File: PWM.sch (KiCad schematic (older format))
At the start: 11 parts, among them U2 MCP6004

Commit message: Rev A
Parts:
- R10: value 43k -> 30k
- R11: value 24k -> 15k
- R8: value 24k -> 30k
- RV1: value 10k -> 100
- RV2: value 10k -> 1k
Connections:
- net VCC: now also R10.1; no longer RV2.1, RV2.2
- net VIN: now also R8.1; no longer RV1.1, RV1.2
- net VIN_DIV: now also RV1.2; no longer R8.2, R9.1
- net VREF: now also RV2.2; no longer R10.2, R11.1
- net BUF_OUT renamed BUF
- net VIN_ADJ renamed VIN_ADJ_M
- net VIN_ADJ_M: now also R9.1; no longer R8.1
- net VREF_ADJ renamed VREF_ADJ_M
- net VREF_ADJ_M: now also R11.1; no longer R10.1
- new net VIN_ADJ_P: R8.2, RV1.1
- new net VREF_ADJ_P: R10.2, RV2.1
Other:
- moved on the sheet: R10, R8, R9, RV1, RV2
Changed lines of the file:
@@
 Text HLabel 5150 1400 0    60   Input ~ 0
 SAWTOOTH
-Text HLabel 2300 1750 0    60   Input ~ 0
+Text HLabel 2300 1800 0    60   Input ~ 0
 VIN
 $Comp
@@
 AR Path="/59C03855/59C00B33" Ref="R35"  Part="1"
 F 0 "R11" V 3230 2400 50  0000 C CNN
-F 1 "24k" V 3150 2400 50  0000 C CNN
+F 1 "15k" V 3150 2400 50  0000 C CNN
 F 2 "olof:R_0805_HandSoldering" V 3080 2400 50  0001 C CNN
 F 3 "" H 3150 2400 50  0000 C CNN
@@
 L R R10
 U 1 1 59C00B88
-P 3150 2000
+P 3150 950
 AR Path="/59C00A8D/59C00B88" Ref="R10"  Part="1"
 AR Path="/59C037F5/59C00B88" Ref="R18"  Part="1"
 AR Path="/59C0381C/59C00B88" Ref="R26"  Part="1"
 AR Path="/59C03855/59C00B88" Ref="R34"  Part="1"
-F 0 "R10" V 3230 2000 50  0000 C CNN
-F 1 "43k" V 3150 2000 50  0000 C CNN
-F 2 "olof:R_0805_HandSoldering" V 3080 2000 50  0001 C CNN
-F 3 "" H 3150 2000 50  0000 C CNN
-F 4 "1208710" V 3150 2000 60  0001 C CNN "Part"
-	1    3150 2000
-	1    0    0    -1
-$EndComp
-Wire Wire Line
-	3150 2150 3150 2250
+F 0 "R10" V 3230 950 50  0000 C CNN
+F 1 "30k" V 3150 950 50  0000 C CNN
+F 2 "olof:R_0805_HandSoldering" V 3080 950 50  0001 C CNN
+F 3 "" H 3150 950 50  0000 C CNN
+F 4 "1208710" V 3150 950 60  0001 C CNN "Part"
+	1    3150 950
+	1    0    0    -1
+$EndComp
+Wire Wire Line
+	3150 1750 3150 2250
 $Comp
 L GND #PWR040
 U 1 1 59C00BB9
-P 3150 2600
+P 3150 2650
 AR Path="/59C00A8D/59C00BB9" Ref="#PWR040"  Part="1"
 AR Path="/59C037F5/59C00BB9" Ref="#PWR047"  Part="1"
 AR Path="/59C0381C/59C00BB9" Ref="#PWR054"  Part="1"
 AR Path="/59C03855/59C00BB9" Ref="#PWR061"  Part="1"
-F 0 "#PWR061" H 3150 2350 50  0001 C CNN
-F 1 "GND" H 3150 2450 50  0000 C CNN
-F 2 "" H 3150 2600 50  0000 C CNN
-F 3 "" H 3150 2600 50  0000 C CNN
-	1    3150 2600
+F 0 "#PWR040" H 3150 2400 50  0001 C CNN
+F 1 "GND" H 3150 2500 50  0000 C CNN
+F 2 "" H 3150 2650 50  0000 C CNN
+F 3 "" H 3150 2650 50  0000 C CNN
+	1    3150 2650
 	1    0    0    -1
 $EndComp
@@
 L VCC #PWR041
 U 1 1 59C00BD3
-P 3150 1100
+P 3150 750
 AR Path="/59C00A8D/59C00BD3" Ref="#PWR041"  Part="1"
 AR Path="/59C037F5/59C00BD3" Ref="#PWR048"  Part="1"
 AR Path="/59C0381C/59C00BD3" Ref="#PWR055"  Part="1"
 AR Path="/59C03855/59C00BD3" Ref="#PWR062"  Part="1"
-F 0 "#PWR062" H 3150 950 50  0001 C CNN
-F 1 "VCC" H 3150 1250 50  0000 C CNN
-F 2 "" H 3150 1100 50  0000 C CNN
-F 3 "" H 3150 1100 50  0000 C CNN
-	1    3150 1100
-	1    0    0    -1
-$EndComp
-Wire Wire Line
-	3150 1500 3150 1850
-Wire Wire Line
-	3150 2550 3150 2600
-Wire Wire Line
-	3150 2200 3750 2200
-Wire Wire Line
-	3750 2200 3750 2750
+F 0 "#PWR041" H 3150 600 50  0001 C CNN
+F 1 "VCC" H 3150 900 50  0000 C CNN
+F 2 "" H 3150 750 50  0000 C CNN
+F 3 "" H 3150 750 50  0000 C CNN
+	1    3150 750
+	1    0    0    -1
+$EndComp
+Wire Wire Line
+	3150 2550 3150 2650
+Wire Wire Line
+	3750 1600 3750 2750
 Wire Wire Line
 	3750 2750 4050 2750
-Connection ~ 3150 2200
 $Comp
 L R R8
 U 1 1 59C00D17
-P 2500 2750
+P 2500 2100
 AR Path="/59C00A8D/59C00D17" Ref="R8"  Part="1"
 AR Path="/59C037F5/59C00D17" Ref="R16"  Part="1"
 AR Path="/59C0381C/59C00D17" Ref="R24"  Part="1"
 AR Path="/59C03855/59C00D17" Ref="R32"  Part="1"
-F 0 "R8" V 2580 2750 50  0000 C CNN
-F 1 "24k" V 2500 2750 50  0000 C CNN
-F 2 "olof:R_0805_HandSoldering" V 2430 2750 50  0001 C CNN
-F 3 "" H 2500 2750 50  0000 C CNN
-	1    2500 2750
+F 0 "R8" V 2580 2100 50  0000 C CNN
+F 1 "30k" V 2500 2100 50  0000 C CNN
+F 2 "olof:R_0805_HandSoldering" V 2430 2100 50  0001 C CNN
+F 3 "" H 2500 2100 50  0000 C CNN
+	1    2500 2100
 	1    0    0    -1
 $EndComp
@@
 L R R9
 U 1 1 59C00DEF
-P 2500 3150
+P 2500 3700
 AR Path="/59C00A8D/59C00DEF" Ref="R9"  Part="1"
 AR Path="/59C037F5/59C00DEF" Ref="R17"  Part="1"
 AR Path="/59C0381C/59C00DEF" Ref="R25"  Part="1"
 AR Path="/59C03855/59C00DEF" Ref="R33"  Part="1"
-F 0 "R9" V 2580 3150 50  0000 C CNN
-F 1 "470" V 2500 3150 50  0000 C CNN
-F 2 "olof:R_0805_HandSoldering" V 2430 3150 50  0001 C CNN
-F 3 "" H 2500 3150 50  0000 C CNN
-F 4 "1208662" V 2500 3150 60  0001 C CNN "Part"
-	1    2500 3150
-	1    0    0    -1
-$EndComp
-Wire Wire Line
-	2500 2900 2500 3000
-Connection ~ 2500 2950
+F 0 "R9" V 2580 3700 50  0000 C CNN
+F 1 "470" V 2500 3700 50  0000 C CNN
+F 2 "olof:R_0805_HandSoldering" V 2430 3700 50  0001 C CNN
+F 3 "" H 2500 3700 50  0000 C CNN
+F 4 "1208662" V 2500 3700 60  0001 C CNN "Part"
+	1    2500 3700
+	1    0    0    -1
+$EndComp
 $Comp
 L GND #PWR042
 U 1 1 59C00E40
-P 2500 3350
+P 2500 3900
 AR Path="/59C00A8D/59C00E40" Ref="#PWR042"  Part="1"
 AR Path="/59C037F5/59C00E40" Ref="#PWR049"  Part="1"
 AR Path="/59C0381C/59C00E40" Ref="#PWR056"  Part="1"
 AR Path="/59C03855/59C00E40" Ref="#PWR063"  Part="1"
-F 0 "#PWR063" H 2500 3100 50  0001 C CNN
-F 1 "GND" H 2500 3200 50  0000 C CNN
-F 2 "" H 2500 3350 50  0000 C CNN
-F 3 "" H 2500 3350 50  0000 C CNN
-	1    2500 3350
-	1    0    0    -1
-$EndComp
-Wire Wire Line
-	2500 3300 2500 3350
-Wire Wire Line
-	2500 2300 2500 2600
+F 0 "#PWR042" H 2500 3650 50  0001 C CNN
+F 1 "GND" H 2500 3750 50  0000 C CNN
+F 2 "" H 2500 3900 50  0000 C CNN
+F 3 "" H 2500 3900 50  0000 C CNN
+	1    2500 3900
+	1    0    0    -1
+$EndComp
+Wire Wire Line
+	2500 3850 2500 3900
 $Comp
 L VCC #PWR043
@@
 AR Path="/59C0381C/59C00F65" Ref="#PWR057"  Part="1"
 AR Path="/59C03855/59C00F65" Ref="#PWR064"  Part="1"
-F 0 "#PWR064" H 4250 2350 50  0001 C CNN
+F 0 "#PWR043" H 4250 2350 50  0001 C CNN
 F 1 "VCC" H 4250 2650 50  0000 C CNN
 F 2 "" H 4250 2500 50  0000 C CNN
@@
 AR Path="/59C0381C/59C00F93" Ref="#PWR058"  Part="1"
 AR Path="/59C03855/59C00F93" Ref="#PWR065"  Part="1"
-F 0 "#PWR065" H 4250 2950 50  0001 C CNN
+F 0 "#PWR044" H 4250 2950 50  0001 C CNN
 F 1 "GND" H 4250 3050 50  0000 C CNN
 F 2 "" H 4250 3200 50  0000 C CNN
@@
 $EndComp
 Wire Wire Line
-	3000 2950 2500 2950
-Wire Wire Line
 	3300 2950 4050 2950
 $Comp
@@
 	5000 2850 5000 3550
 Wire Wire Line
-	5000 3550 4400 3550
+	4400 3550 7100 3550
 $Comp
 L MCP6004 U2
@@
 AR Path="/59C0381C/59C015C7" Ref="#PWR059"  Part="1"
 AR Path="/59C03855/59C015C7" Ref="#PWR066"  Part="1"
-F 0 "#PWR066" H 5850 2250 50  0001 C CNN
+F 0 "#PWR045" H 5850 2250 50  0001 C CNN
 F 1 "VCC" H 5850 2550 50  0000 C CNN
 F 2 "" H 5850 2400 50  0000 C CNN
@@
 AR Path="/59C0381C/59C0160F" Ref="#PWR060"  Part="1"
 AR Path="/59C03855/59C0160F" Ref="#PWR067"  Part="1"
-F 0 "#PWR067" H 5850 2850 50  0001 C CNN
+F 0 "#PWR046" H 5850 2850 50  0001 C CNN
 F 1 "GND" H 5850 2950 50  0000 C CNN
 F 2 "" H 5850 3100 50  0000 C CNN
@@
 L POT RV2
 U 1 1 59C01D1D
-P 3150 1350
+P 3150 1600
 AR Path="/59C00A8D/59C01D1D" Ref="RV2"  Part="1"
 AR Path="/59C037F5/59C01D1D" Ref="RV4"  Part="1"
 AR Path="/59C0381C/59C01D1D" Ref="RV6"  Part="1"
 AR Path="/59C03855/59C01D1D" Ref="RV8"  Part="1"
-F 0 "RV2" H 3150 1270 50  0000 C CNN
-F 1 "10k" H 3150 1350 50  0000 C CNN
-F 2 "olof:Potentiometer_Bourns_3386P" H 3150 1350 50  0001 C CNN
-F 3 "" H 3150 1350 50  0000 C CNN
-	1    3150 1350
-	0    1    1    0
-$EndComp
-Wire Wire Line
-	3150 1100 3150 1200
-Wire Wire Line
-	3150 1150 3400 1150
-Wire Wire Line
-	3400 1150 3400 1350
-Wire Wire Line
-	3400 1350 3300 1350
-Connection ~ 3150 1150
+F 0 "RV2" H 3150 1520 50  0000 C CNN
+F 1 "1k" H 3150 1600 50  0000 C CNN
+F 2 "olof:Potentiometer_Bourns_3386P" H 3150 1600 50  0001 C CNN
+F 3 "" H 3150 1600 50  0000 C CNN
+	1    3150 1600
+	0    1    1    0
+$EndComp
+Wire Wire Line
+	3150 750  3150 800
 $Comp
 L POT RV1
 U 1 1 59C02178
-P 2500 2150
+P 2500 2950
 AR Path="/59C00A8D/59C02178" Ref="RV1"  Part="1"
 AR Path="/59C037F5/59C02178" Ref="RV3"  Part="1"
 AR Path="/59C0381C/59C02178" Ref="RV5"  Part="1"
 AR Path="/59C03855/59C02178" Ref="RV7"  Part="1"
-F 0 "RV1" H 2500 2070 50  0000 C CNN
-F 1 "10k" H 2500 2150 50  0000 C CNN
-F 2 "olof:Potentiometer_Bourns_3386P" H 2500 2150 50  0001 C CNN
-F 3 "" H 2500 2150 50  0000 C CNN
-	1    2500 2150
-	0    1    1    0
-$EndComp
-Wire Wire Line
-	2650 2150 2750 2150
-Wire Wire Line
-	2750 2150 2750 1900
-Wire Wire Line
-	2750 1900 2500 1900
-Wire Wire Line
-	2300 1750 2500 1750
-Connection ~ 2500 1900
+F 0 "RV1" H 2500 2870 50  0000 C CNN
+F 1 "100" H 2500 2950 50  0000 C CNN
+F 2 "olof:Potentiometer_Bourns_3386P" H 2500 2950 50  0001 C CNN
+F 3 "" H 2500 2950 50  0000 C CNN
+	1    2500 2950
+	0    1    1    0
+$EndComp
+Wire Wire Line
+	2300 1800 2500 1800
 Text Label 5400 2500 1    40   ~ 0
 SAW_P
-Text Label 3400 2200 0    40   ~ 0
+Text Label 3450 1600 0    40   ~ 0
 VREF
 Text Label 2700 2950 0    40   ~ 0
 VIN_DIV
-Wire Wire Line
-	2500 1750 2500 2000
-Text Label 2500 2550 1    40   ~ 0
-VIN_ADJ
-Text Label 3150 1800 1    40   ~ 0
-VREF_ADJ
+Text Label 2500 2400 3    40   ~ 0
+VIN_ADJ_P
+Text Label 3150 1450 1    40   ~ 0
+VREF_ADJ_P
 Text Label 3450 2950 0    40   ~ 0
 BUF_IN
 Text Label 4650 3550 0    40   ~ 0
 BUF_OUT
+Wire Wire Line
+	3000 2950 2650 2950
+Wire Wire Line
+	2500 3100 2500 3550
+Wire Wire Line
+	2500 2250 2500 2800
+Wire Wire Line
+	2500 1800 2500 1950
+Text Label 2500 3200 3    40   ~ 0
+VIN_ADJ_M
+Wire Wire Line
+	3150 1100 3150 1450
+Text Label 3150 2200 1    40   ~ 0
+VREF_ADJ_M
+Wire Wire Line
+	3750 1600 3300 1600
+Text HLabel 7100 3550 2    60   Output ~ 0
+BUF
+Connection ~ 5000 3550
 $EndSCHEMATC

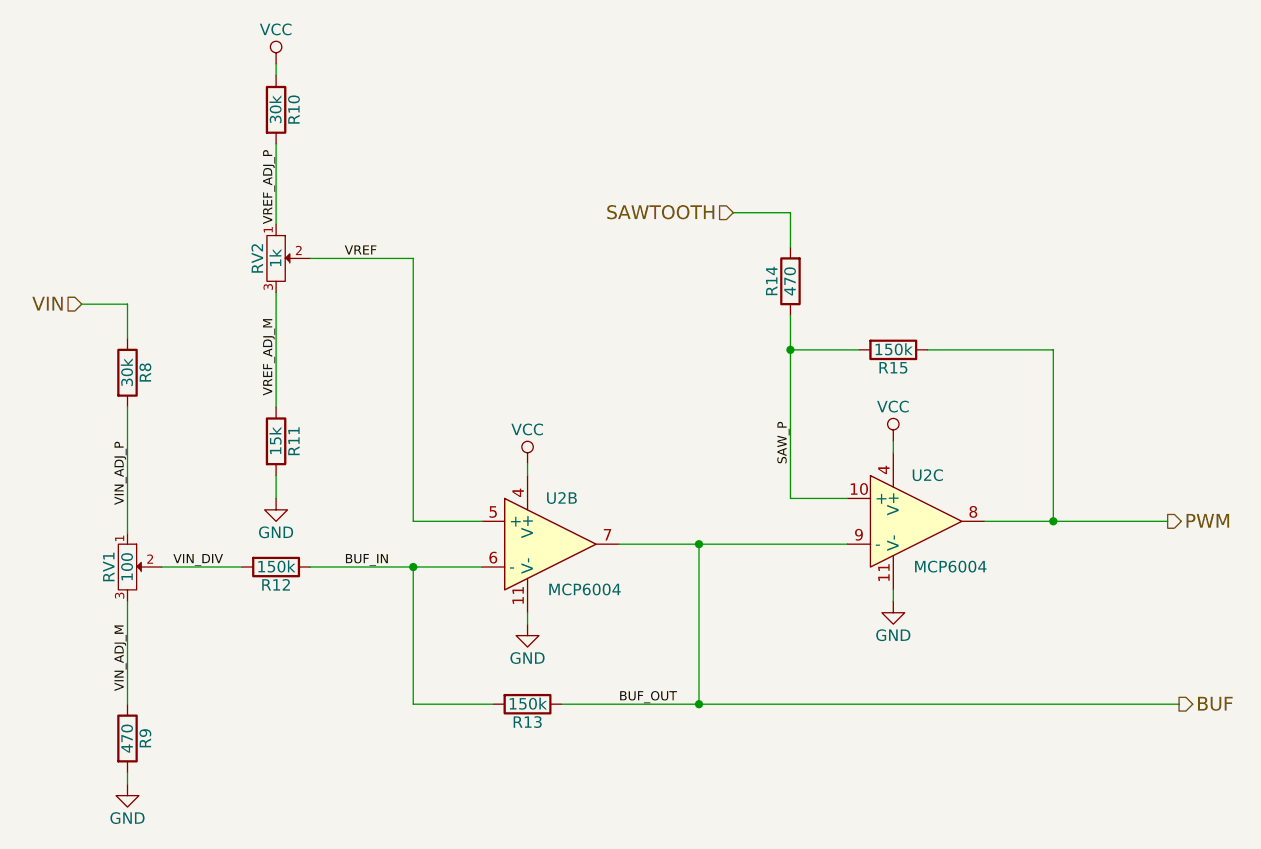
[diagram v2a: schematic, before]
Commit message: Removed 0R resistors and started new layout
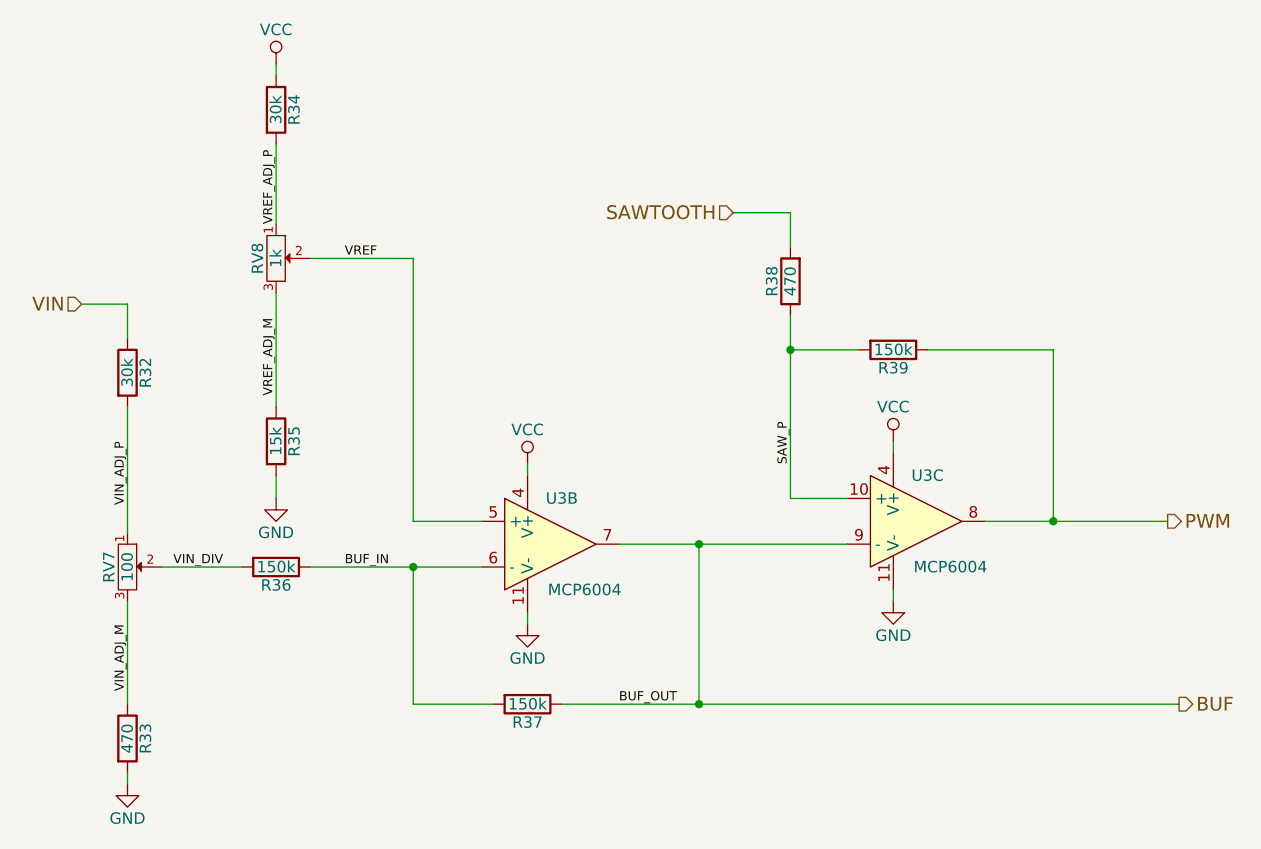
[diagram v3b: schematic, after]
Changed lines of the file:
@@
 AR Path="/59C0381C/59C00AA1" Ref="U3"  Part="1"
 AR Path="/59C03855/59C00AA1" Ref="U3"  Part="2"
-F 0 "U2" H 4400 3050 50  0000 C CNN
+F 0 "U3" H 4400 3050 50  0000 C CNN
 F 1 "MCP6004" H 4500 2650 50  0000 C CNN
 F 2 "olof:SOIC-14_3.9x8.7mm_Pitch1.27mm" H 4300 2950 50  0001 C CNN
@@
 AR Path="/59C0381C/59C00B33" Ref="R27"  Part="1"
 AR Path="/59C03855/59C00B33" Ref="R35"  Part="1"
-F 0 "R11" V 3230 2400 50  0000 C CNN
+F 0 "R35" V 3230 2400 50  0000 C CNN
 F 1 "15k" V 3150 2400 50  0000 C CNN
 F 2 "olof:R_0805_HandSoldering" V 3080 2400 50  0001 C CNN
@@
 AR Path="/59C0381C/59C00B88" Ref="R26"  Part="1"
 AR Path="/59C03855/59C00B88" Ref="R34"  Part="1"
-F 0 "R10" V 3230 950 50  0000 C CNN
+F 0 "R34" V 3230 950 50  0000 C CNN
 F 1 "30k" V 3150 950 50  0000 C CNN
 F 2 "olof:R_0805_HandSoldering" V 3080 950 50  0001 C CNN
@@
 	3150 1750 3150 2250
 $Comp
-L GND #PWR023
+L GND #PWR033
 U 1 1 59C00BB9
 P 3150 2650
-AR Path="/59C00A8D/59C00BB9" Ref="#PWR023"  Part="1"
-AR Path="/59C037F5/59C00BB9" Ref="#PWR030"  Part="1"
-AR Path="/59C0381C/59C00BB9" Ref="#PWR037"  Part="1"
-AR Path="/59C03855/59C00BB9" Ref="#PWR044"  Part="1"
-F 0 "#PWR044" H 3150 2400 50  0001 C CNN
+AR Path="/59C00A8D/59C00BB9" Ref="#PWR033"  Part="1"
+AR Path="/59C037F5/59C00BB9" Ref="#PWR040"  Part="1"
+AR Path="/59C0381C/59C00BB9" Ref="#PWR047"  Part="1"
+AR Path="/59C03855/59C00BB9" Ref="#PWR054"  Part="1"
+F 0 "#PWR054" H 3150 2400 50  0001 C CNN
 F 1 "GND" H 3150 2500 50  0000 C CNN
 F 2 "" H 3150 2650 50  0000 C CNN
@@
 $EndComp
 $Comp
-L VCC #PWR024
+L VCC #PWR034
 U 1 1 59C00BD3
 P 3150 750
-AR Path="/59C00A8D/59C00BD3" Ref="#PWR024"  Part="1"
-AR Path="/59C037F5/59C00BD3" Ref="#PWR031"  Part="1"
-AR Path="/59C0381C/59C00BD3" Ref="#PWR038"  Part="1"
-AR Path="/59C03855/59C00BD3" Ref="#PWR045"  Part="1"
-F 0 "#PWR045" H 3150 600 50  0001 C CNN
+AR Path="/59C00A8D/59C00BD3" Ref="#PWR034"  Part="1"
+AR Path="/59C037F5/59C00BD3" Ref="#PWR041"  Part="1"
+AR Path="/59C0381C/59C00BD3" Ref="#PWR048"  Part="1"
+AR Path="/59C03855/59C00BD3" Ref="#PWR055"  Part="1"
+F 0 "#PWR055" H 3150 600 50  0001 C CNN
 F 1 "VCC" H 3150 900 50  0000 C CNN
 F 2 "" H 3150 750 50  0000 C CNN
@@
 AR Path="/59C0381C/59C00D17" Ref="R24"  Part="1"
 AR Path="/59C03855/59C00D17" Ref="R32"  Part="1"
-F 0 "R8" V 2580 2100 50  0000 C CNN
+F 0 "R32" V 2580 2100 50  0000 C CNN
 F 1 "30k" V 2500 2100 50  0000 C CNN
 F 2 "olof:R_0805_HandSoldering" V 2430 2100 50  0001 C CNN
@@
 AR Path="/59C0381C/59C00DEF" Ref="R25"  Part="1"
 AR Path="/59C03855/59C00DEF" Ref="R33"  Part="1"
-F 0 "R9" V 2580 3700 50  0000 C CNN
+F 0 "R33" V 2580 3700 50  0000 C CNN
 F 1 "470" V 2500 3700 50  0000 C CNN
 F 2 "olof:R_0805_HandSoldering" V 2430 3700 50  0001 C CNN
@@
 $EndComp
 $Comp
-L GND #PWR025
+L GND #PWR035
 U 1 1 59C00E40
 P 2500 3900
-AR Path="/59C00A8D/59C00E40" Ref="#PWR025"  Part="1"
-AR Path="/59C037F5/59C00E40" Ref="#PWR032"  Part="1"
-AR Path="/59C0381C/59C00E40" Ref="#PWR039"  Part="1"
-AR Path="/59C03855/59C00E40" Ref="#PWR046"  Part="1"
-F 0 "#PWR046" H 2500 3650 50  0001 C CNN
+AR Path="/59C00A8D/59C00E40" Ref="#PWR035"  Part="1"
+AR Path="/59C037F5/59C00E40" Ref="#PWR042"  Part="1"
+AR Path="/59C0381C/59C00E40" Ref="#PWR049"  Part="1"
+AR Path="/59C03855/59C00E40" Ref="#PWR056"  Part="1"
+F 0 "#PWR056" H 2500 3650 50  0001 C CNN
 F 1 "GND" H 2500 3750 50  0000 C CNN
 F 2 "" H 2500 3900 50  0000 C CNN
@@
 	2500 3850 2500 3900
 $Comp
-L VCC #PWR026
+L VCC #PWR036
 U 1 1 59C00F65
 P 4250 2500
-AR Path="/59C00A8D/59C00F65" Ref="#PWR026"  Part="1"
-AR Path="/59C037F5/59C00F65" Ref="#PWR033"  Part="1"
-AR Path="/59C0381C/59C00F65" Ref="#PWR040"  Part="1"
-AR Path="/59C03855/59C00F65" Ref="#PWR047"  Part="1"
-F 0 "#PWR047" H 4250 2350 50  0001 C CNN
+AR Path="/59C00A8D/59C00F65" Ref="#PWR036"  Part="1"
+AR Path="/59C037F5/59C00F65" Ref="#PWR043"  Part="1"
+AR Path="/59C0381C/59C00F65" Ref="#PWR050"  Part="1"
+AR Path="/59C03855/59C00F65" Ref="#PWR057"  Part="1"
+F 0 "#PWR057" H 4250 2350 50  0001 C CNN
 F 1 "VCC" H 4250 2650 50  0000 C CNN
 F 2 "" H 4250 2500 50  0000 C CNN
@@
 	4250 2500 4250 2550
 $Comp
-L GND #PWR027
+L GND #PWR037
 U 1 1 59C00F93
 P 4250 3200
-AR Path="/59C00A8D/59C00F93" Ref="#PWR027"  Part="1"
-AR Path="/59C037F5/59C00F93" Ref="#PWR034"  Part="1"
-AR Path="/59C0381C/59C00F93" Ref="#PWR041"  Part="1"
-AR Path="/59C03855/59C00F93" Ref="#PWR048"  Part="1"
-F 0 "#PWR048" H 4250 2950 50  0001 C CNN
+AR Path="/59C00A8D/59C00F93" Ref="#PWR037"  Part="1"
+AR Path="/59C037F5/59C00F93" Ref="#PWR044"  Part="1"
+AR Path="/59C0381C/59C00F93" Ref="#PWR051"  Part="1"
+AR Path="/59C03855/59C00F93" Ref="#PWR058"  Part="1"
+F 0 "#PWR058" H 4250 2950 50  0001 C CNN
 F 1 "GND" H 4250 3050 50  0000 C CNN
 F 2 "" H 4250 3200 50  0000 C CNN
@@
 AR Path="/59C0381C/59C00FC9" Ref="R28"  Part="1"
 AR Path="/59C03855/59C00FC9" Ref="R36"  Part="1"
-F 0 "R12" V 3230 2950 50  0000 C CNN
+F 0 "R36" V 3230 2950 50  0000 C CNN
 F 1 "150k" V 3150 2950 50  0000 C CNN
 F 2 "olof:R_0805_HandSoldering" V 3080 2950 50  0001 C CNN
@@
 AR Path="/59C0381C/59C01032" Ref="R29"  Part="1"
 AR Path="/59C03855/59C01032" Ref="R37"  Part="1"
-F 0 "R13" V 4330 3550 50  0000 C CNN
+F 0 "R37" V 4330 3550 50  0000 C CNN
 F 1 "150k" V 4250 3550 50  0000 C CNN
 F 2 "olof:R_0805_HandSoldering" V 4180 3550 50  0001 C CNN
@@
 AR Path="/59C0381C/59C014A7" Ref="U3"  Part="4"
 AR Path="/59C03855/59C014A7" Ref="U3"  Part="3"
-F 0 "U2" H 6000 2950 50  0000 C CNN
+F 0 "U3" H 6000 2950 50  0000 C CNN
 F 1 "MCP6004" H 6100 2550 50  0000 C CNN
 F 2 "olof:SOIC-14_3.9x8.7mm_Pitch1.27mm" H 5900 2850 50  0001 C CNN
@@
 AR Path="/59C0381C/59C0154A" Ref="R31"  Part="1"
 AR Path="/59C03855/59C0154A" Ref="R39"  Part="1"
-F 0 "R15" V 5930 2000 50  0000 C CNN
+F 0 "R39" V 5930 2000 50  0000 C CNN
 F 1 "150k" V 5850 2000 50  0000 C CNN
 F 2 "olof:R_0805_HandSoldering" V 5780 2000 50  0001 C CNN
@@
 $EndComp
 $Comp
-L VCC #PWR028
+L VCC #PWR038
 U 1 1 59C015C7
 P 5850 2400
-AR Path="/59C00A8D/59C015C7" Ref="#PWR028"  Part="1"
-AR Path="/59C037F5/59C015C7" Ref="#PWR035"  Part="1"
-AR Path="/59C0381C/59C015C7" Ref="#PWR042"  Part="1"
-AR Path="/59C03855/59C015C7" Ref="#PWR049"  Part="1"
-F 0 "#PWR049" H 5850 2250 50  0001 C CNN
+AR Path="/59C00A8D/59C015C7" Ref="#PWR038"  Part="1"
+AR Path="/59C037F5/59C015C7" Ref="#PWR045"  Part="1"
+AR Path="/59C0381C/59C015C7" Ref="#PWR052"  Part="1"
+AR Path="/59C03855/59C015C7" Ref="#PWR059"  Part="1"
+F 0 "#PWR059" H 5850 2250 50  0001 C CNN
 F 1 "VCC" H 5850 2550 50  0000 C CNN
 F 2 "" H 5850 2400 50  0000 C CNN
@@
 	5850 2400 5850 2450
 $Comp
-L GND #PWR029
+L GND #PWR039
 U 1 1 59C0160F
 P 5850 3100
-AR Path="/59C00A8D/59C0160F" Ref="#PWR029"  Part="1"
-AR Path="/59C037F5/59C0160F" Ref="#PWR036"  Part="1"
-AR Path="/59C0381C/59C0160F" Ref="#PWR043"  Part="1"
-AR Path="/59C03855/59C0160F" Ref="#PWR050"  Part="1"
-F 0 "#PWR050" H 5850 2850 50  0001 C CNN
+AR Path="/59C00A8D/59C0160F" Ref="#PWR039"  Part="1"
+AR Path="/59C037F5/59C0160F" Ref="#PWR046"  Part="1"
+AR Path="/59C0381C/59C0160F" Ref="#PWR053"  Part="1"
+AR Path="/59C03855/59C0160F" Ref="#PWR060"  Part="1"
+F 0 "#PWR060" H 5850 2850 50  0001 C CNN
 F 1 "GND" H 5850 2950 50  0000 C CNN
 F 2 "" H 5850 3100 50  0000 C CNN
@@
 AR Path="/59C0381C/59C016AF" Ref="R30"  Part="1"
 AR Path="/59C03855/59C016AF" Ref="R38"  Part="1"
-F 0 "R14" V 5480 1700 50  0000 C CNN
+F 0 "R38" V 5480 1700 50  0000 C CNN
 F 1 "470" V 5400 1700 50  0000 C CNN
 F 2 "olof:R_0805_HandSoldering" V 5330 1700 50  0001 C CNN
@@
 AR Path="/59C0381C/59C01D1D" Ref="RV6"  Part="1"
 AR Path="/59C03855/59C01D1D" Ref="RV8"  Part="1"
-F 0 "RV2" H 3150 1520 50  0000 C CNN
+F 0 "RV8" H 3150 1520 50  0000 C CNN
 F 1 "1k" H 3150 1600 50  0000 C CNN
 F 2 "olof:Potentiometer_Bourns_3386P" H 3150 1600 50  0001 C CNN
@@
 AR Path="/59C0381C/59C02178" Ref="RV5"  Part="1"
 AR Path="/59C03855/59C02178" Ref="RV7"  Part="1"
-F 0 "RV1" H 2500 2870 50  0000 C CNN
+F 0 "RV7" H 2500 2870 50  0000 C CNN
 F 1 "100" H 2500 2950 50  0000 C CNN
 F 2 "olof:Potentiometer_Bourns_3386P" H 2500 2950 50  0001 C CNN
